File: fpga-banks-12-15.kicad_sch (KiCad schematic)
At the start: 1 part, among them U3002 XC7K160T-FFG676

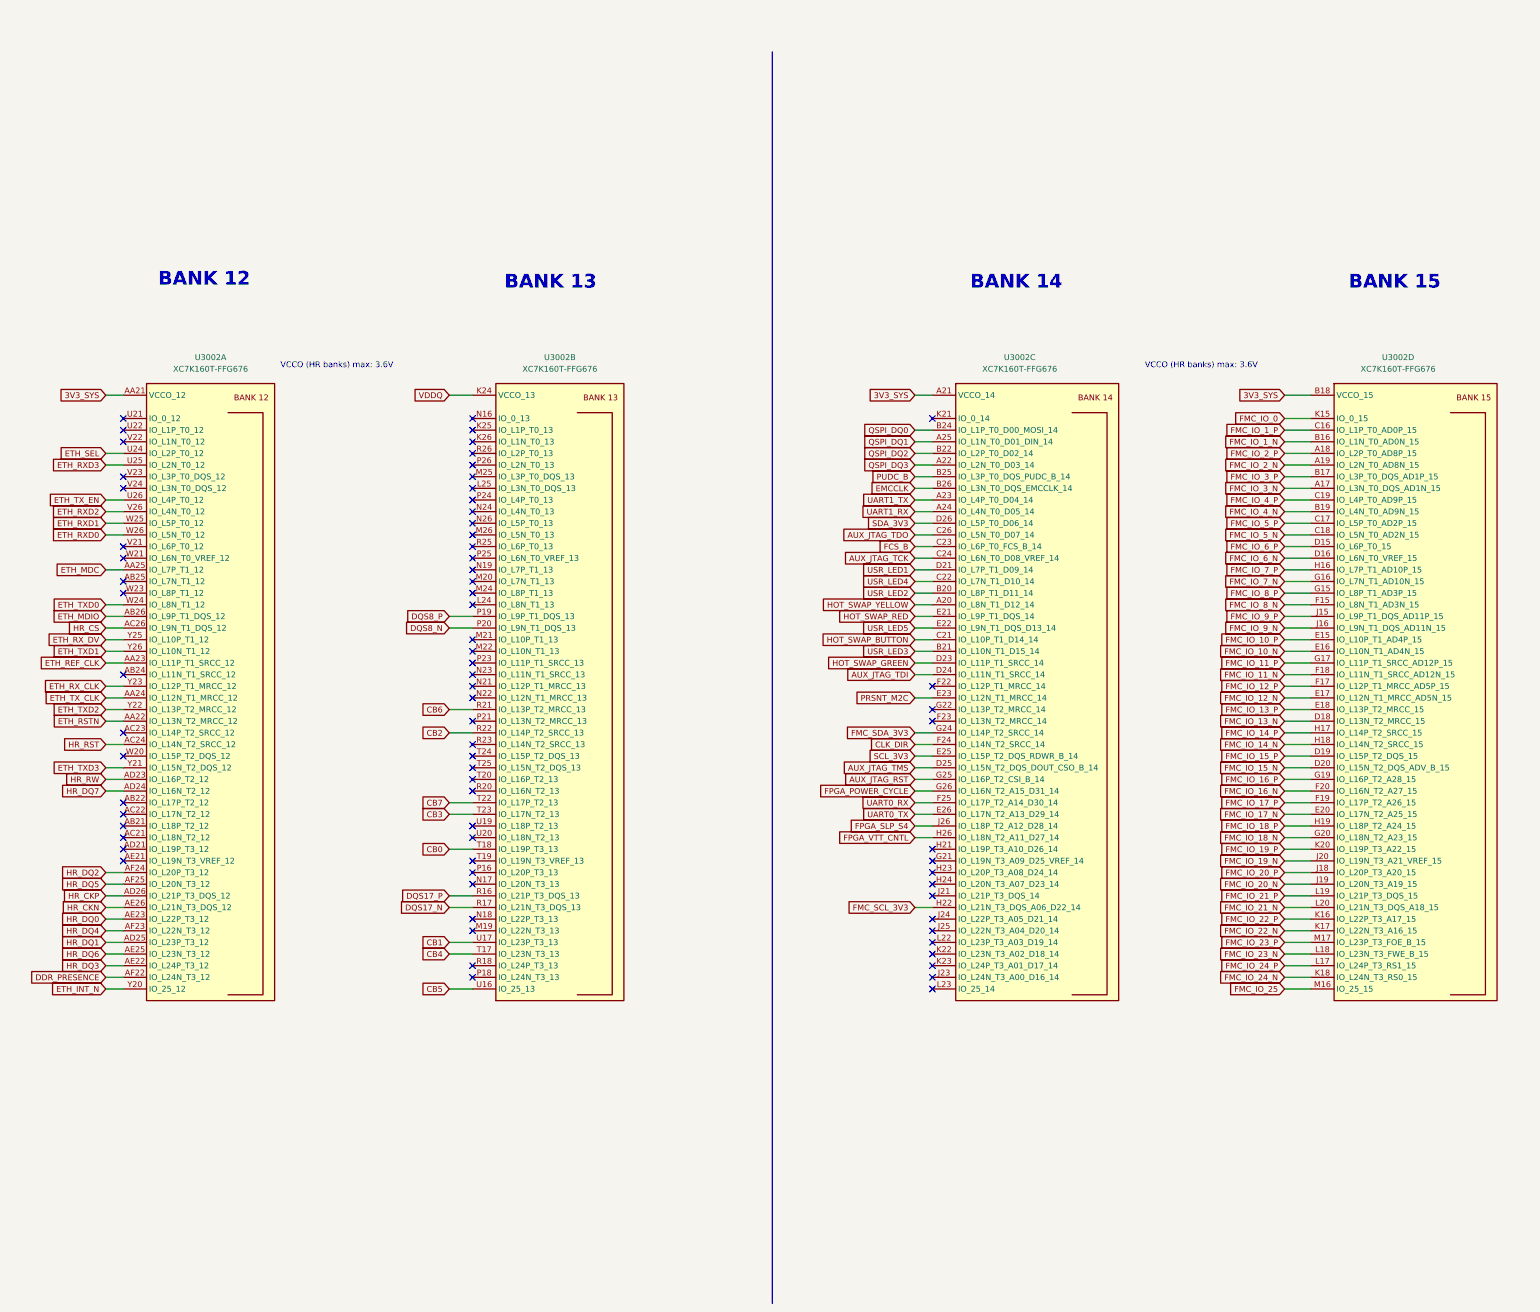
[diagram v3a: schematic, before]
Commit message: Replace supply labels with proper symbols
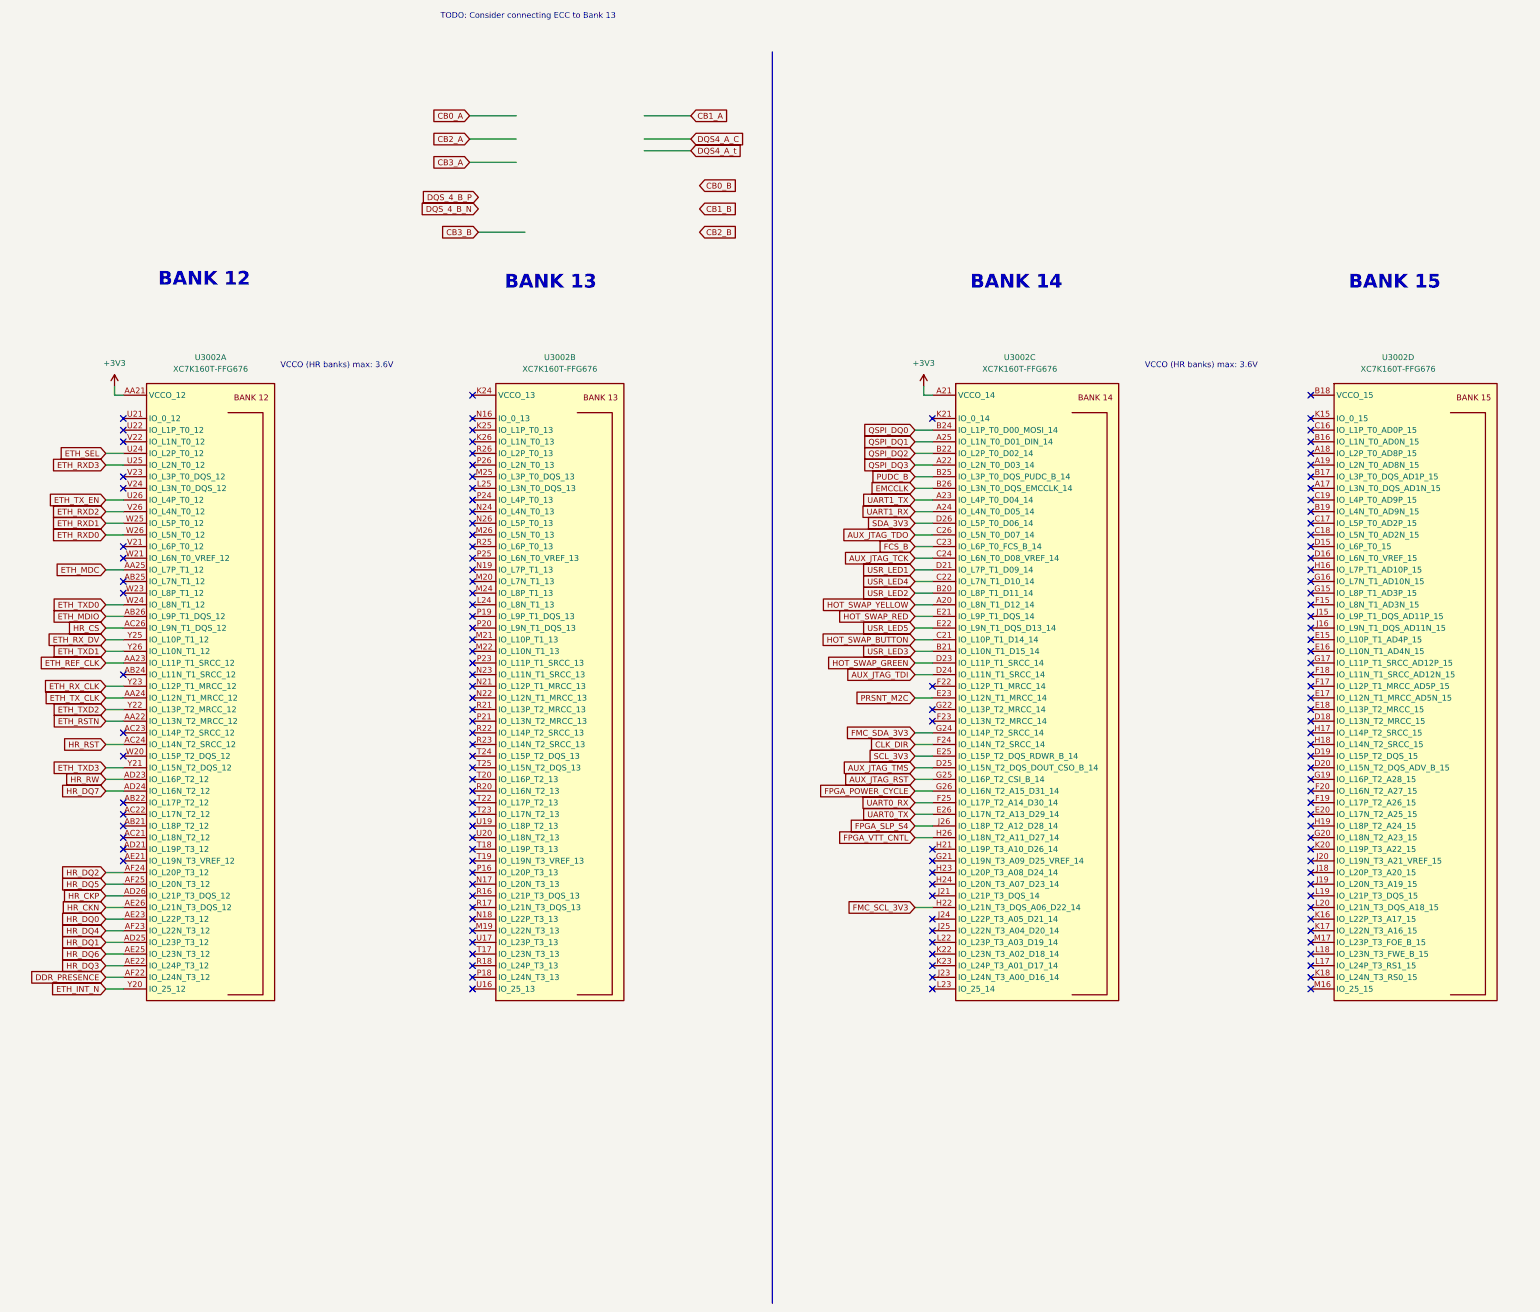
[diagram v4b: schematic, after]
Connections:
- net 3V3_SYS renamed +3V3
- net +3V3: no longer U3002.B18 (VCCO_15), U3002.E19 (VCCO_15), U3002.F16 (VCCO_15), U3002.H20 (VCCO_15), U3002.J17 (VCCO_15), U3002.M18 (VCCO_15)
- net CB0: no longer names the net of U3002.T18 (IO_L19P_T3_13)
- net CB1: no longer names the net of U3002.U17 (IO_L23P_T3_13)
- net CB2: no longer names the net of U3002.R22 (IO_L14P_T2_SRCC_13)
- net CB3: no longer names the net of U3002.T23 (IO_L17N_T2_13)
- net CB4: no longer names the net of U3002.T17 (IO_L23N_T3_13)
- net CB5: no longer names the net of U3002.U16 (IO_25_13)
- net CB6: no longer names the net of U3002.R21 (IO_L13P_T2_MRCC_13)
- net CB7: no longer names the net of U3002.T22 (IO_L17P_T2_13)
- net DQS17_N: no longer names the net of U3002.R17 (IO_L21N_T3_DQS_13)
- net DQS17_P: no longer names the net of U3002.R16 (IO_L21P_T3_DQS_13)
- net DQS8_N: no longer names the net of U3002.P20 (IO_L9N_T1_DQS_13)
- net DQS8_P: no longer names the net of U3002.P19 (IO_L9P_T1_DQS_13)
- net FMC_IO_0: no longer names the net of U3002.K15 (IO_0_15)
- net FMC_IO_10_N: no longer names the net of U3002.E16 (IO_L10N_T1_AD4N_15)
- net FMC_IO_10_P: no longer names the net of U3002.E15 (IO_L10P_T1_AD4P_15)
- net FMC_IO_11_N: no longer names the net of U3002.F18 (IO_L11N_T1_SRCC_AD12N_15)
- net FMC_IO_11_P: no longer names the net of U3002.G17 (IO_L11P_T1_SRCC_AD12P_15)
- net FMC_IO_12_N: no longer names the net of U3002.E17 (IO_L12N_T1_MRCC_AD5N_15)
- net FMC_IO_12_P: no longer names the net of U3002.F17 (IO_L12P_T1_MRCC_AD5P_15)
- net FMC_IO_13_N: no longer names the net of U3002.D18 (IO_L13N_T2_MRCC_15)
- net FMC_IO_13_P: no longer names the net of U3002.E18 (IO_L13P_T2_MRCC_15)
- net FMC_IO_14_N: no longer names the net of U3002.H18 (IO_L14N_T2_SRCC_15)
- net FMC_IO_14_P: no longer names the net of U3002.H17 (IO_L14P_T2_SRCC_15)
- net FMC_IO_15_N: no longer names the net of U3002.D20 (IO_L15N_T2_DQS_ADV_B_15)
- net FMC_IO_15_P: no longer names the net of U3002.D19 (IO_L15P_T2_DQS_15)
- net FMC_IO_16_N: no longer names the net of U3002.F20 (IO_L16N_T2_A27_15)
- net FMC_IO_16_P: no longer names the net of U3002.G19 (IO_L16P_T2_A28_15)
- net FMC_IO_17_N: no longer names the net of U3002.E20 (IO_L17N_T2_A25_15)
- net FMC_IO_17_P: no longer names the net of U3002.F19 (IO_L17P_T2_A26_15)
- net FMC_IO_18_N: no longer names the net of U3002.G20 (IO_L18N_T2_A23_15)
- net FMC_IO_18_P: no longer names the net of U3002.H19 (IO_L18P_T2_A24_15)
- net FMC_IO_19_N: no longer names the net of U3002.J20 (IO_L19N_T3_A21_VREF_15)
- net FMC_IO_19_P: no longer names the net of U3002.K20 (IO_L19P_T3_A22_15)
- net FMC_IO_1_N: no longer names the net of U3002.B16 (IO_L1N_T0_AD0N_15)
- net FMC_IO_1_P: no longer names the net of U3002.C16 (IO_L1P_T0_AD0P_15)
- net FMC_IO_20_N: no longer names the net of U3002.J19 (IO_L20N_T3_A19_15)
- net FMC_IO_20_P: no longer names the net of U3002.J18 (IO_L20P_T3_A20_15)
- net FMC_IO_21_N: no longer names the net of U3002.L20 (IO_L21N_T3_DQS_A18_15)
- net FMC_IO_21_P: no longer names the net of U3002.L19 (IO_L21P_T3_DQS_15)
- net FMC_IO_22_N: no longer names the net of U3002.K17 (IO_L22N_T3_A16_15)
- net FMC_IO_22_P: no longer names the net of U3002.K16 (IO_L22P_T3_A17_15)
- net FMC_IO_23_N: no longer names the net of U3002.L18 (IO_L23N_T3_FWE_B_15)
- net FMC_IO_23_P: no longer names the net of U3002.M17 (IO_L23P_T3_FOE_B_15)
- net FMC_IO_24_N: no longer names the net of U3002.K18 (IO_L24N_T3_RS0_15)
- net FMC_IO_24_P: no longer names the net of U3002.L17 (IO_L24P_T3_RS1_15)
- net FMC_IO_25: no longer names the net of U3002.M16 (IO_25_15)
- net FMC_IO_2_N: no longer names the net of U3002.A19 (IO_L2N_T0_AD8N_15)
- net FMC_IO_2_P: no longer names the net of U3002.A18 (IO_L2P_T0_AD8P_15)
- net FMC_IO_3_N: no longer names the net of U3002.A17 (IO_L3N_T0_DQS_AD1N_15)
- net FMC_IO_3_P: no longer names the net of U3002.B17 (IO_L3P_T0_DQS_AD1P_15)
- net FMC_IO_4_N: no longer names the net of U3002.B19 (IO_L4N_T0_AD9N_15)
- net FMC_IO_4_P: no longer names the net of U3002.C19 (IO_L4P_T0_AD9P_15)
- net FMC_IO_5_N: no longer names the net of U3002.C18 (IO_L5N_T0_AD2N_15)
- net FMC_IO_5_P: no longer names the net of U3002.C17 (IO_L5P_T0_AD2P_15)
- net FMC_IO_6_N: no longer names the net of U3002.D16 (IO_L6N_T0_VREF_15)
- net FMC_IO_6_P: no longer names the net of U3002.D15 (IO_L6P_T0_15)
- net FMC_IO_7_N: no longer names the net of U3002.G16 (IO_L7N_T1_AD10N_15)
- net FMC_IO_7_P: no longer names the net of U3002.H16 (IO_L7P_T1_AD10P_15)
- net FMC_IO_8_N: no longer names the net of U3002.F15 (IO_L8N_T1_AD3N_15)
- net FMC_IO_8_P: no longer names the net of U3002.G15 (IO_L8P_T1_AD3P_15)
- net FMC_IO_9_N: no longer names the net of U3002.J16 (IO_L9N_T1_DQS_AD11N_15)
- net FMC_IO_9_P: no longer names the net of U3002.J15 (IO_L9P_T1_DQS_AD11P_15)
- net VDDQ: no longer names the net of U3002.K24 (VCCO_13), U3002.N25 (VCCO_13), U3002.P22 (VCCO_13), U3002.R19 (VCCO_13), U3002.T16 (VCCO_13), U3002.T26 (VCCO_13)
- new net: U3002.B18 (VCCO_15), U3002.E19 (VCCO_15), U3002.F16 (VCCO_15), U3002.H20 (VCCO_15), U3002.J17 (VCCO_15), U3002.M18 (VCCO_15)
- no-connect marks 72 -> 136
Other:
- note added: "TODO: Consider connecting ECC to Bank 13"
